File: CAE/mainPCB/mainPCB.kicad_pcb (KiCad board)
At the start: 2 copper layers, 150 x 100 mm, 28 parts, among them J1 DHT22_CVT, J10 V_in_01, J12 LORA, J13 GPS_NEO, J14 VL6180X_01, J15 VL6180X_02, J2 V_In, J3 LM3144_CVT, J4 LM3144_RPM, J5 DS18B20_01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

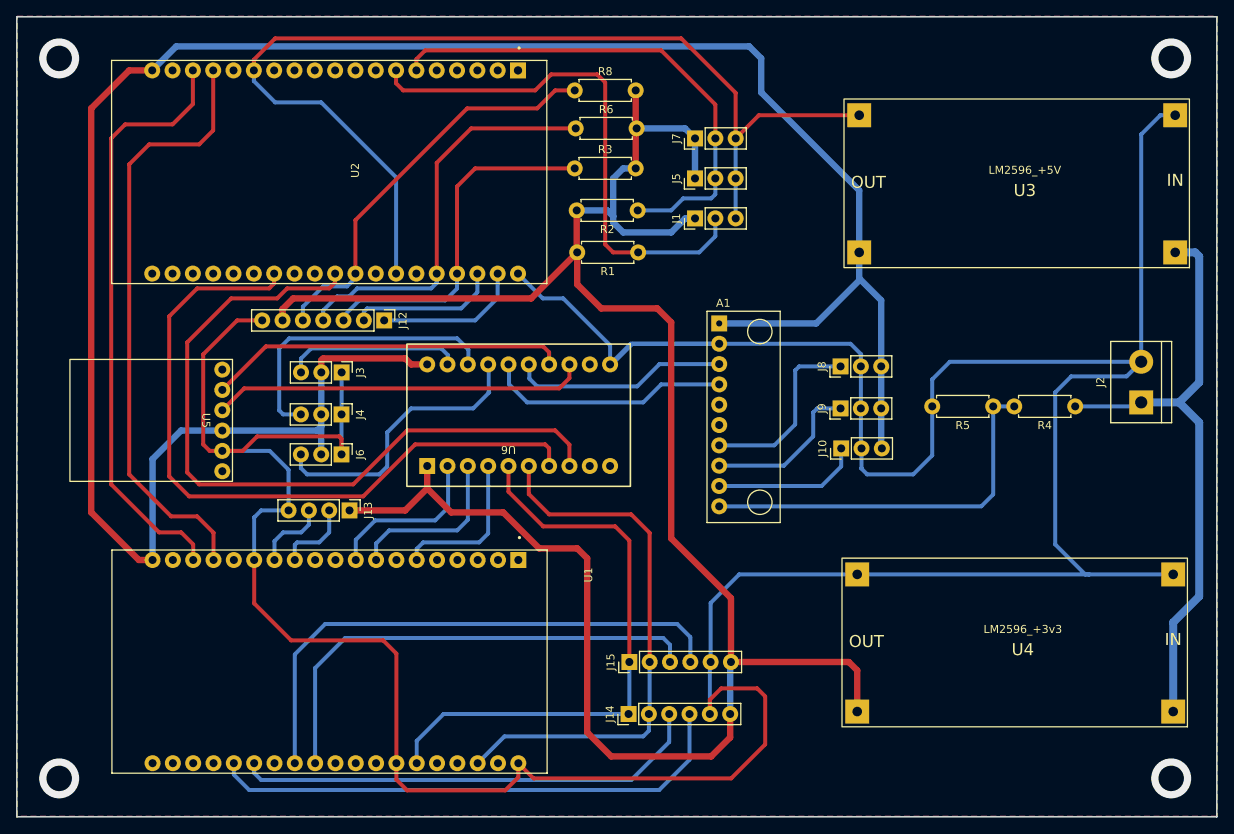
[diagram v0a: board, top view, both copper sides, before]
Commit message: PCB updated
3D models added, rewiring for milling
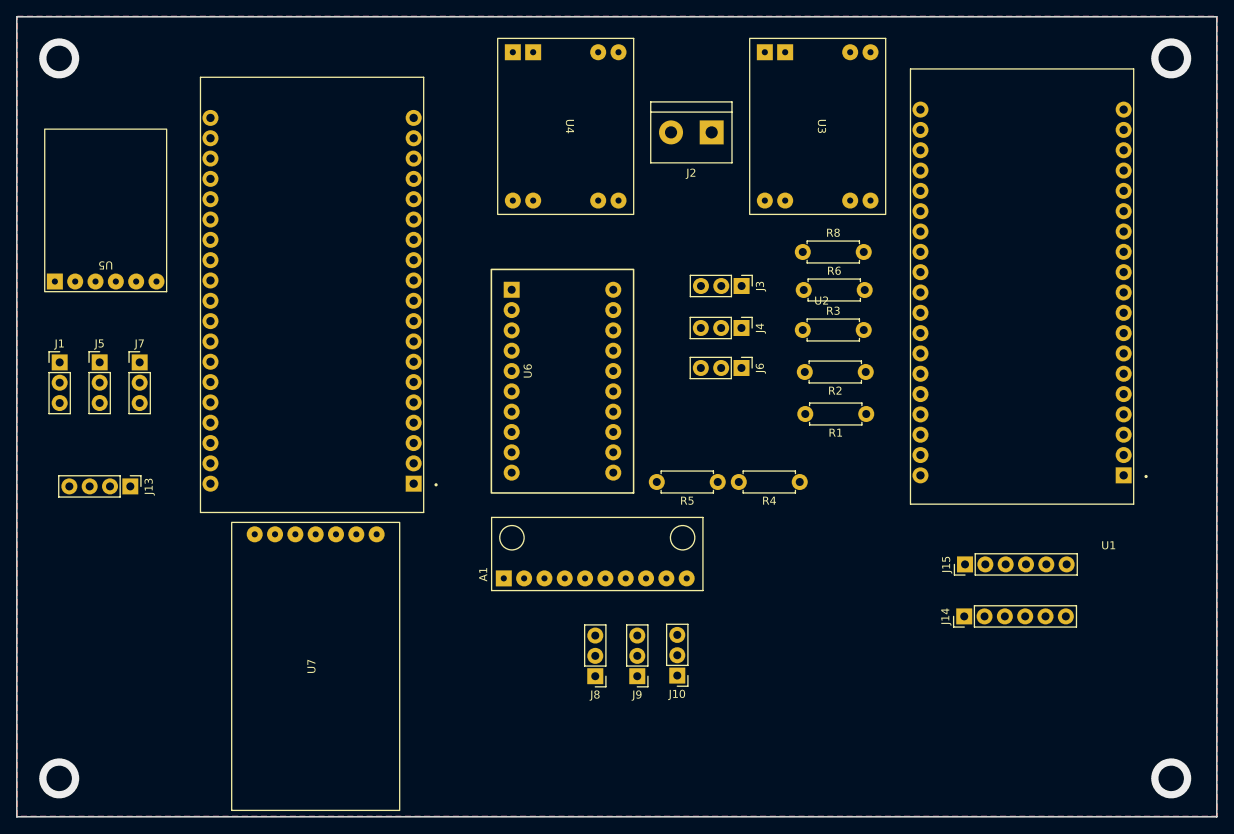
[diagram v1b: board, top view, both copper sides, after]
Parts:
- removed J12: LORA, Connector_PinHeader_2.54mm:PinHeader_1x07_P2.54mm_Vertical
- added U7: Lora e22, custom:lora_e22, F.Cu at (102.8, 134.0)
- U3: value LM2596_+5V -> MP1584EN 3V3; footprint DC_DC_LM2596_small:DC_DC_LM2596_small -> custom:MP1584EN
- U4: value LM2596_+3v3 -> MP1584EN 5V; footprint DC_DC_LM2596_small:DC_DC_LM2596_small -> custom:MP1584EN
- moved U1 97.4 mm to (191.1, 87.3), turned to 180 degrees
- moved U4 94.4 mm to (134.0, 66.5), turned to -90 degrees
- moved J1 81.4 mm to (70.8, 96.0), turned to 0 degrees
- moved J5 77.9 mm to (75.8, 96.0), turned to 0 degrees
- moved J7 74.9 mm to (80.8, 96.0), turned to 0 degrees
- moved J2 63.4 mm to (152.2, 67.2), turned to 180 degrees
- moved J3 51.1 mm to (156.0, 86.5)
- moved J4 51.1 mm to (156.0, 91.7)
- moved J6 51.1 mm to (156.0, 96.7)
- moved J8 49.4 mm to (137.7, 135.2), turned to 180 degrees
- moved U3 44.7 mm to (165.5, 66.5), turned to -90 degrees
- moved J14 43.7 mm to (183.8, 127.8)
- moved J15 43.7 mm to (183.9, 121.2)
- moved J9 42.0 mm to (142.9, 135.2), turned to 180 degrees
- moved A1 41.7 mm to (126.3, 123.0), turned to 90 degrees
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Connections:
- U3 pad 3: +5V -> +3V3
- U4 pad 3: +3V3 -> +5V
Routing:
- net GND: track 588.4 -> 0.00 mm
- net +5V: track 283.7 -> 0.00 mm
- net +3V3: track 281.0 -> 0.00 mm
- net RX_OpenLog_L: track 93.6 -> 0.00 mm
- net TX_OpenLog_L: track 89.7 -> 0.00 mm
- net V_Bat: track 76.7 -> 0.00 mm
- net RX_ESP32: track 75.5 -> 0.00 mm
- net TX_ESP32: track 74.8 -> 0.00 mm
- net SDA_01_L: track 73.2 -> 0.00 mm
- net SLC_01_L: track 68.5 -> 0.00 mm
- net SHDN_04: track 68.4 -> 0.00 mm
- net Net-(J1-Pin_2): track 66.9 -> 0.00 mm
- net SHDN_02: track 66.5 -> 0.00 mm
- net Net-(J5-Pin_2): track 63.8 -> 0.00 mm
- net SHDN_03: track 60.3 -> 0.00 mm
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
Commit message: PCB design updated
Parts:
- added J11: OpenLog TX, Connector_PinHeader_2.54mm:PinHeader_1x02_P2.54mm_Vertical, F.Cu at (82.9, 103.0)
- added J12: MPU6050_1, Connector_PinHeader_2.54mm:PinHeader_1x04_P2.54mm_Vertical, F.Cu at (176.0, 111.9)
- added Q1: BSS138, Package_TO_SOT_SMD:SOT-23, F.Cu at (75.2, 90.8)
- added Q2: BSS138, Package_TO_SOT_SMD:SOT-23, F.Cu at (75.3, 96.7)
- added R10: R10K, Resistor_THT:R_Axial_DIN0207_L6.3mm_D2.5mm_P7.62mm_Horizontal, F.Cu at (76.2, 110.9)
- added R11: R10K, Resistor_THT:R_Axial_DIN0207_L6.3mm_D2.5mm_P7.62mm_Horizontal, F.Cu at (81.8, 87.2)
- added R7: R10K, Resistor_THT:R_Axial_DIN0207_L6.3mm_D2.5mm_P7.62mm_Horizontal, F.Cu at (71.2, 110.8)
- added R9: R10K, Resistor_THT:R_Axial_DIN0207_L6.3mm_D2.5mm_P7.62mm_Horizontal, F.Cu at (70.5, 85.4)
- added U8: Neo GPS, custom:neo_gps, F.Cu at (192.5, 131.2)
- J13: value GPS_NEO -> MPU6050_2
- moved R8 82.7 mm to (101.3, 136.5), turned to 180 degrees
- moved R6 77.1 mm to (101.3, 132.2), turned to 180 degrees
- moved R2 72.9 mm to (102.3, 120.0)
- moved R3 71.5 mm to (102.3, 128.8), turned to 180 degrees
- moved J7 58.6 mm to (139.2, 92.7)
- moved J5 56.6 mm to (132.2, 92.7)
- moved J14 55.6 mm to (176.8, 72.6), turned to 180 degrees
- moved J1 54.6 mm to (125.2, 92.7)
- moved R1 49.1 mm to (125.2, 86.2), turned to 0 degrees
- moved J13 47.1 mm to (119.8, 86.9), turned to 0 degrees
- moved R4 38.5 mm to (149.5, 74.9), turned to -90 degrees
- moved J3 35.6 mm to (170.3, 119.0), turned to 180 degrees
- moved R5 30.0 mm to (144.0, 82.3), turned to 90 degrees
- moved J4 28.6 mm to (164.3, 119.0), turned to 180 degrees
- moved J15 27.4 mm to (176.8, 94.8), turned to 180 degrees
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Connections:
- J13 pad 2: RX_GPS -> SLC_02_L
- J13 pad 3: TX_GPS -> SDA_02_L
- U1 pad 12: RX_GPS -> unconnected-(U1-14-Pad12)
- U1 pad 13: TX_GPS -> unconnected-(U1-12-Pad13)
- U1 pad 16: RX_ESP32 -> unconnected-(U1-D2-Pad16)
- U1 pad 17: TX_ESP32 -> unconnected-(U1-D3-Pad17)
- U1 pad 27: unconnected-(U1-19-Pad27) -> TX_GPS
- U1 pad 28: unconnected-(U1-18-Pad28) -> RX_GPS
- U2 pad 10: unconnected-(U2-26-Pad10) -> SDA_02_L
- U2 pad 11: unconnected-(U2-27-Pad11) -> SLC_02_L
- U2 pad 16: RX_ESP32 -> unconnected-(U2-D2-Pad16)
- U2 pad 17: TX_ESP32 -> unconnected-(U2-D3-Pad17)
- U2 pad 21: M0 -> M1
- U2 pad 22: M1 -> SLC_01_L
- U2 pad 23: RX_LORA -> Net-(Q1-S)
- U2 pad 24: TX_LORA -> Net-(J11-Pin_1)
- U2 pad 25: unconnected-(U2-21-Pad25) -> SDA_01_L
- U2 pad 29: RX_OpenLog_L -> unconnected-(U2-5-Pad29)
- U2 pad 30: unconnected-(U2-17-Pad30) -> RX_LORA
- U2 pad 31: unconnected-(U2-16-Pad31) -> TX_LORA
- U2 pad 32: TX_OpenLog_L -> unconnected-(U2-4-Pad32)
- U2 pad 6: Net-(J5-Pin_2) -> unconnected-(U2-35-Pad6)
- U2 pad 8: unconnected-(U2-33-Pad8) -> Net-(J5-Pin_2)
- U2 pad 9: unconnected-(U2-25-Pad9) -> M0
- U5 pad 4: TX_OpenLog_H -> Net-(Q2-D)
- U5 pad 5: RX_OpenLog_H -> Net-(Q1-D)
- U6 pad 13: TX_OpenLog_H -> unconnected-(U6-B7-Pad13)
- U6 pad 14: RX_OpenLog_H -> unconnected-(U6-B6-Pad14)
- U6 pad 7: TX_OpenLog_L -> unconnected-(U6-A6-Pad7)
- U6 pad 8: RX_OpenLog_L -> unconnected-(U6-A7-Pad8)
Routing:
- net +5V: track 0.00 -> 455.8 mm
- net GND: track 0.00 -> 400.0 mm
- net +3V3: track 0.00 -> 390.6 mm, vias 0 -> 3
- net SLC_01_L: track 0.00 -> 215.3 mm, vias 0 -> 1
- net SDA_01_L: track 0.00 -> 194.2 mm
- net Net-(U1-35): track 0.00 -> 86.1 mm
- net Net-(U1-33): track 0.00 -> 83.9 mm
- net 1/3_V_Bat: track 0.00 -> 79.7 mm, vias 0 -> 1
- net Net-(U1-25): track 0.00 -> 79.4 mm
- net Net-(J5-Pin_2): track 0.00 -> 71.0 mm
- net RX_LORA: track 0.00 -> 69.4 mm, vias 0 -> 1
- net AUX_LORA: track 0.00 -> 66.9 mm, vias 0 -> 1
- net TX_LORA: track 0.00 -> 62.2 mm, vias 0 -> 1
- net RX_GPS: track 0.00 -> 53.1 mm
- net V_Bat: track 0.00 -> 51.5 mm
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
